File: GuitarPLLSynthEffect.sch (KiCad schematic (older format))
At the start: 15 parts

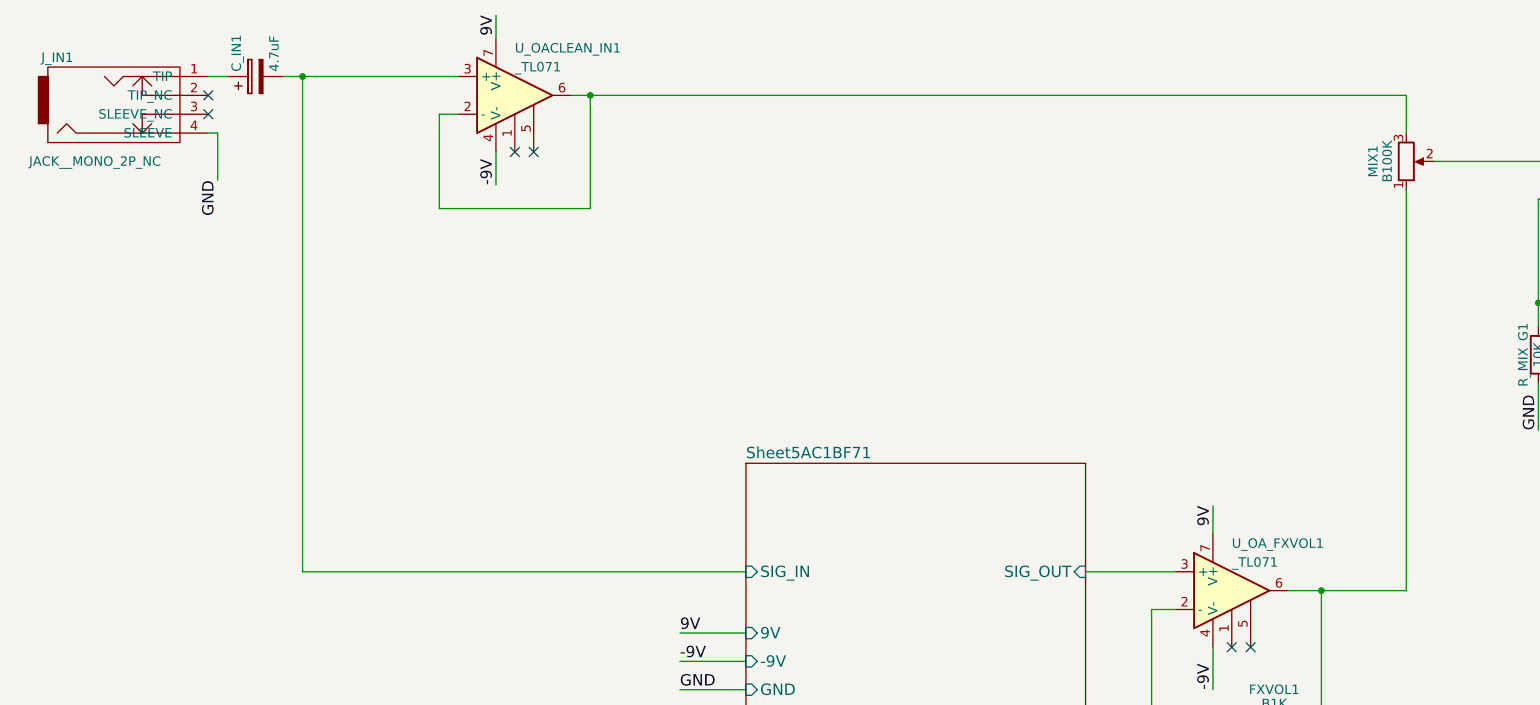
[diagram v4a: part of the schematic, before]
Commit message: schematic design update
Added clean signal input and selector switch (dirty signal will always go to mixer)
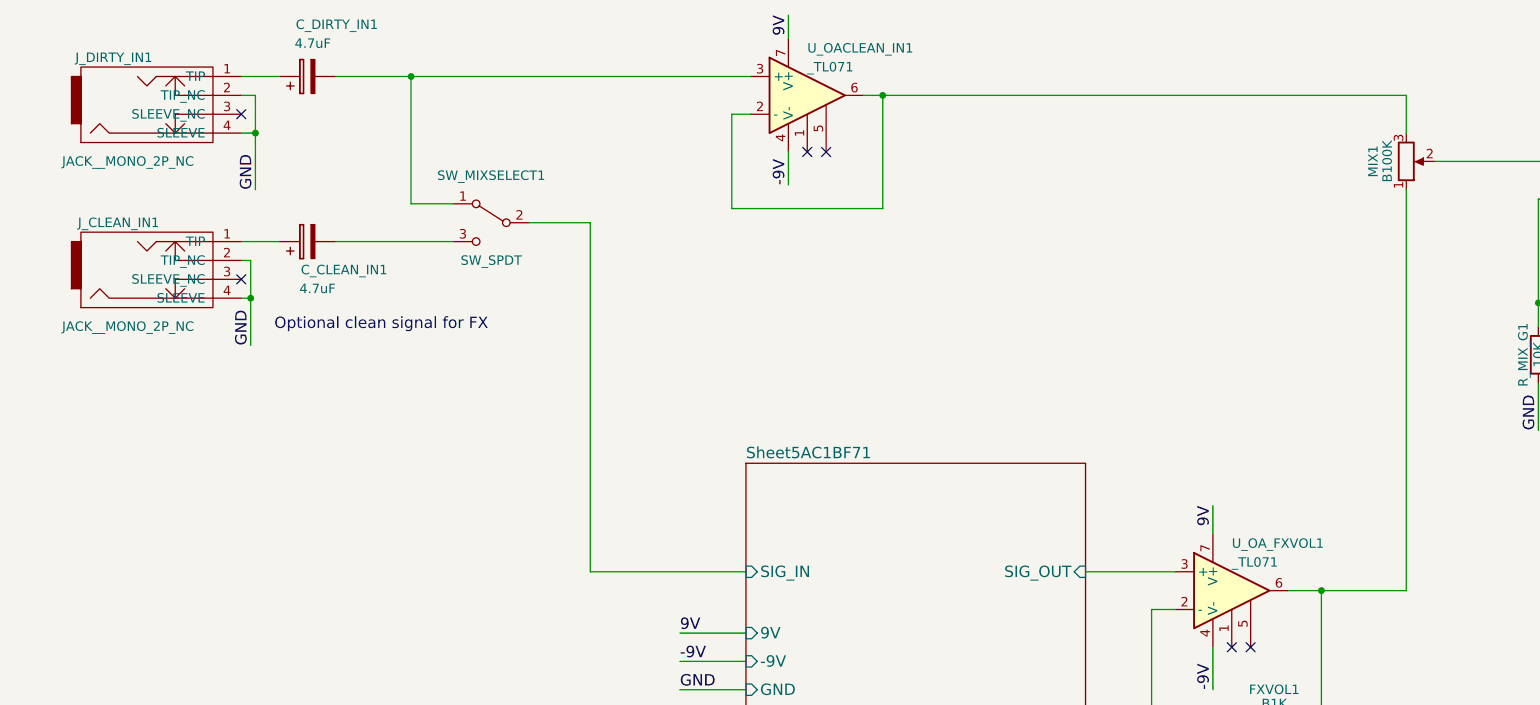
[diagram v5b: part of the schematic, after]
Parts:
- added C_DIRTY_IN1: 4.7uF, symbol CP
- added J_DIRTY_IN1: JACK__MONO_2P_NC, symbol JACK__MONO_2P_NC
- added SW_MIXSELECT1: SW_SPDT, symbol SW_SPDT
- renumbered C_IN1 to C_CLEAN_IN1, J_IN1 to J_CLEAN_IN1
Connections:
- net GND: now also J_CLEAN_IN1.2 (TIP_NC), J_DIRTY_IN1.2 (TIP_NC), J_DIRTY_IN1.4 (SLEEVE)
- net Sheet5AC1BF71/SIG_IN: now also SW_MIXSELECT1.2 (B); no longer C_CLEAN_IN1.2, U_OACLEAN_IN1.3 (+)
- new net: C_CLEAN_IN1.2, SW_MIXSELECT1.3 (C)
- new net: C_DIRTY_IN1.2, SW_MIXSELECT1.1 (A), U_OACLEAN_IN1.3 (+)
- new net: C_DIRTY_IN1.1, J_DIRTY_IN1.1 (TIP)
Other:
- note added: "Optional clean signal for FX"
- moved on the sheet: C_CLEAN_IN1, J_CLEAN_IN1, U_OACLEAN_IN1

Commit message: Final RevA Schematic
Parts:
- added C_RIP1: 100nF, Capacitors_SMD:CP_Elec_4x5.3, symbol C
- added D_IN1: _Schottky, Diodes_SMD:D_SOD-123F, symbol _Schottky
- added D_ON1: LED, LEDs:LED_D5.0mm, symbol LED
- added J_AUX2MAIN_INSW1, J_MAIN2AUX_INSW1: Conn_01x04, Pin_Headers:Pin_Header_Straight_1x04_Pitch2.54mm, symbol Conn_01x04
- added J_AUX2MAIN_VOL1, J_MAIN2AUX_VOL1: Conn_01x06, Pin_Headers:Pin_Header_Straight_1x06_Pitch2.54mm, symbol Conn_01x06
- added SW_BYPASS1: SW_3PDT_on_on, custom_sw:SW_3PDT_W18MM_L17.3MM_P5.3MM_D2MM_PCBPin, symbol SW_3PDT_on_on
- C1_NEG1: renamed from C_NEG2; footprint (none) -> Capacitors_SMD:CP_Elec_4x5.3
- C2_NEG1: renamed from C_NEG1; footprint (none) -> Capacitors_SMD:CP_Elec_4x5.3
- C_CLEAN_IN1, C_DIRTY_IN1: footprint (none) -> Capacitors_SMD:C_0805_HandSoldering
- FXVOL1, MIX1: footprint (none) -> Potentiometers:Potentiometer_Bourns_PTV09A-1_Horizontal
- J_CLEAN_IN1, J_DIRTY_IN1, J_OU1: footprint (none) -> custom_sockets:JackSocket_Mono_PCB
- J_POWER1: footprint (none) -> custom_sockets:BARREL_JACK
- R_FXVOL1, R_MIX_F1, R_MIX_G1: footprint (none) -> Resistors_SMD:R_0805_HandSoldering
- SW_INSW1: renamed from SW_MIXSELECT1; footprint (none) -> custom_sw:SW_SPDT_W6.86MM_L12.7MM_P4.8MM_D2MM
- U_NEG1, U_OACLEAN_IN1, U_OA_FXVOL1, U_OA_MIX1: footprint (none) -> SMD_Packages:SOIC-8-N
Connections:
- net 9V: now also D_IN1.1 (K), SW_BYPASS1.8 (B); no longer J_POWER1.1
- net GND: now also J_POWER1.1, C_RIP1.2, D_ON1.1 (K); no longer J_POWER1.2
- net at SW_INSW1.3 (C): now also J_AUX2MAIN_INSW1.3 (Pin_3); no longer C_CLEAN_IN1.2
- net at U_OA_MIX1.3 (+): now also SW_BYPASS1.5 (B); no longer MIX1.2
- net MIX_P3: now reaches U_OACLEAN_IN1.2 (-), U_OACLEAN_IN1.6
- net MIX_P3: now also J_MAIN2AUX_VOL1.3 (Pin_3); no longer MIX1.3
- net INSW_P1: now reaches C_DIRTY_IN1.2, U_OACLEAN_IN1.3 (+)
- net INSW_P1: now also J_MAIN2AUX_INSW1.1 (Pin_1); no longer SW_INSW1.1 (A)
- net at FXVOL1.1, FXVOL1.2: now also J_AUX2MAIN_VOL1.6 (Pin_6); no longer R_FXVOL1.1, U_OA_FXVOL1.2 (-)
- net at J_DIRTY_IN1.1 (TIP): now also SW_BYPASS1.2 (B); no longer C_DIRTY_IN1.1
- net Sheet5AC1BF71/SIG_IN: no longer names the net of SW_INSW1.2 (B)
- net Sheet5AC1BF71/SIG_IN: now also J_AUX2MAIN_INSW1.2 (Pin_2)
- new net: C_RIP1.1, D_IN1.2 (A), J_POWER1.2
- new net: J_AUX2MAIN_VOL1.1 (Pin_1), MIX1.1
- new net: J_AUX2MAIN_VOL1.2 (Pin_2), MIX1.2
- new net: J_AUX2MAIN_VOL1.3 (Pin_3), MIX1.3
- new net: FXVOL1.3, J_AUX2MAIN_VOL1.5 (Pin_5)
- new net: J_AUX2MAIN_INSW1.1 (Pin_1), SW_INSW1.1 (A)
- new net: C_DIRTY_IN1.1, SW_BYPASS1.3 (C)
- new net: SW_BYPASS1.1 (A), SW_BYPASS1.4 (A)
- new net: D_ON1.2 (A), SW_BYPASS1.9 (C)
- new net FXVOL_P1_2: J_MAIN2AUX_VOL1.6 (Pin_6), R_FXVOL1.1, U_OA_FXVOL1.2 (-)
- new net FXVOL_P3: J_MAIN2AUX_VOL1.1 (Pin_1), J_MAIN2AUX_VOL1.5 (Pin_5), U_OA_FXVOL1.6
- new net INSW_P2: J_MAIN2AUX_INSW1.2 (Pin_2)
- new net INSW_P3: C_CLEAN_IN1.2, J_MAIN2AUX_INSW1.3 (Pin_3)
- new net MIX_P2: J_MAIN2AUX_VOL1.2 (Pin_2), SW_BYPASS1.6 (C)
- no-connect marks 13 -> 18
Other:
- note added: "FX OUTPUT\nVOLUME POT"
- note added: "FX/CLEAN\nBLEND POT"
- note added: "SPDT\nFX INPUT\nSELECTOR"
- moved on the sheet: C1_NEG1, C2_NEG1, C_CLEAN_IN1, C_DIRTY_IN1, FXVOL1, J_CLEAN_IN1, J_DIRTY_IN1, J_OU1, J_POWER1, MIX1, R_FXVOL1, R_MIX_F1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

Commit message: Board Design Update RevA
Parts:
- added C_OABY1, C_OABY2, C_OABY3, C_OABY4, C_OABY5, C_OABY6, C_PWRBY2: 100nF, symbol C
- added J_AUX2MAIN_LED1, J_MAIN2AUX_LED1: Conn_01x04, Pin_Headers:Pin_Header_Straight_1x04_Pitch2.54mm, symbol Conn_01x04
- added R_LED1: 2K7, symbol R
- C_PWRBY1: renamed from C_RIP1; value 100nF -> 10uF
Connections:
- net -9V: now also C_OABY2.1, C_OABY4.1, C_OABY6.1
- net 9V: now also C_OABY1.1, C_OABY3.1, C_OABY5.1
- net GND: now also C_OABY1.2, C_OABY2.2, C_OABY3.2, C_OABY4.2, C_OABY5.2, C_OABY6.2, C_PWRBY2.1, J_MAIN2AUX_LED1.2 (Pin_2); no longer D_ON1.1 (K)
- net at C_PWRBY1.1, D_IN1.2 (A), J_POWER1.2: now also C_PWRBY2.2
- net at D_ON1.2 (A): now also J_AUX2MAIN_LED1.1 (Pin_1); no longer SW_BYPASS1.9 (C)
- new net: J_AUX2MAIN_LED1.2 (Pin_2), R_LED1.2
- new net: D_ON1.1 (K), R_LED1.1
- new net LED_ANODE: J_MAIN2AUX_LED1.1 (Pin_1), SW_BYPASS1.9 (C)
- no-connect marks 18 -> 22
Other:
- moved on the sheet: C1_NEG1, C2_NEG1, C_PWRBY1, D_IN1, D_ON1, J_AUX2MAIN_INSW1, J_MAIN2AUX_INSW1, J_OU1, J_POWER1, R_FXVOL1, R_MIX_F1, R_MIX_G1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

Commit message: update
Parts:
- C_OABY1, C_OABY2, C_OABY3, C_OABY4, C_OABY5, C_OABY6, C_PWRBY2: footprint (none) -> Capacitors_SMD:C_0805_HandSoldering
- C_PWRBY1: footprint Capacitors_SMD:CP_Elec_4x5.3 -> Capacitors_SMD:C_0805_HandSoldering
- R_LED1: footprint (none) -> Resistors_SMD:R_0805_HandSoldering
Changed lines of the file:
@@
 F 0 "C_PWRBY1" H 2075 1700 50  0000 L CNN
 F 1 "10uF" H 2075 1500 50  0000 L CNN
-F 2 "Capacitors_SMD:CP_Elec_4x5.3" H 2088 1450 50  0001 C CNN
+F 2 "Capacitors_SMD:C_0805_HandSoldering" H 2088 1450 50  0001 C CNN
 F 3 "" H 2050 1600 50  0001 C CNN
 	1    2050 1600
@@
 F 0 "R_LED1" V 2655 6475 50  0000 C CNN
 F 1 "2K7" V 2575 6475 50  0000 C CNN
-F 2 "" V 2505 6475 50  0001 C CNN
+F 2 "Resistors_SMD:R_0805_HandSoldering" V 2505 6475 50  0001 C CNN
 F 3 "" H 2575 6475 50  0001 C CNN
 	1    2575 6475
@@
 F 0 "C_OABY1" V 4025 3250 50  0000 L CNN
 F 1 "100nF" V 4100 3250 50  0000 L CNN
-F 2 "" H 4213 3375 50  0001 C CNN
+F 2 "Capacitors_SMD:C_0805_HandSoldering" H 4213 3375 50  0001 C CNN
 F 3 "" H 4175 3525 50  0001 C CNN
 	1    4175 3525
@@
 F 0 "C_OABY5" V 6000 4350 50  0000 L CNN
 F 1 "100nF" V 6075 4350 50  0000 L CNN
-F 2 "" H 6188 4500 50  0001 C CNN
+F 2 "Capacitors_SMD:C_0805_HandSoldering" H 6188 4500 50  0001 C CNN
 F 3 "" H 6150 4650 50  0001 C CNN
 	1    6150 4650
@@
 F 0 "C_OABY3" V 8725 4025 50  0000 L CNN
 F 1 "100nF" V 8800 4025 50  0000 L CNN
-F 2 "" H 8913 4150 50  0001 C CNN
+F 2 "Capacitors_SMD:C_0805_HandSoldering" H 8913 4150 50  0001 C CNN
 F 3 "" H 8875 4300 50  0001 C CNN
 	1    8875 4300
@@
 F 0 "C_OABY2" V 4200 3850 50  0000 L CNN
 F 1 "100nF" V 4275 3850 50  0000 L CNN
-F 2 "" H 4363 3975 50  0001 C CNN
+F 2 "Capacitors_SMD:C_0805_HandSoldering" H 4363 3975 50  0001 C CNN
 F 3 "" H 4325 4125 50  0001 C CNN
 	1    4325 4125
@@
 F 0 "C_OABY4" V 8925 4625 50  0000 L CNN
 F 1 "100nF" V 9000 4625 50  0000 L CNN
-F 2 "" H 9088 4750 50  0001 C CNN
+F 2 "Capacitors_SMD:C_0805_HandSoldering" H 9088 4750 50  0001 C CNN
 F 3 "" H 9050 4900 50  0001 C CNN
 	1    9050 4900
@@
 F 0 "C_OABY6" V 6050 4950 50  0000 L CNN
 F 1 "100nF" V 6125 4950 50  0000 L CNN
-F 2 "" H 6213 5100 50  0001 C CNN
+F 2 "Capacitors_SMD:C_0805_HandSoldering" H 6213 5100 50  0001 C CNN
 F 3 "" H 6175 5250 50  0001 C CNN
 	1    6175 5250
@@
 F 0 "C_PWRBY2" H 2225 1500 50  0000 L CNN
 F 1 "100nF" H 2375 1700 50  0000 L CNN
-F 2 "" H 2663 1450 50  0001 C CNN
+F 2 "Capacitors_SMD:C_0805_HandSoldering" H 2663 1450 50  0001 C CNN
 F 3 "" H 2625 1600 50  0001 C CNN
 	1    2625 1600
